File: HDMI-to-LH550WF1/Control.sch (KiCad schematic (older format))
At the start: 48 parts, among them P4 CONN_02X10, P5 CONN_01X03, U10 FXMA2104UMX, U11 STM32F103C8Tx, U9 FXMA2104UMX, Y1 8MHz

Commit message: C46 should be 0603
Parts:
- C46: footprint Capacitors_SMD:C_0402 -> Capacitors_SMD:C_0603
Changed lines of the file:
@@
 F 0 "C46" H 5710 1270 50  0000 L CNN
 F 1 "4.7uF" H 5710 1120 50  0000 L CNN
-F 2 "Capacitors_SMD:C_0402" H 5700 1200 50  0001 C CNN
+F 2 "Capacitors_SMD:C_0603" H 5700 1200 50  0001 C CNN
 F 3 "" H 5700 1200 50  0000 C CNN
 	1    5700 1200

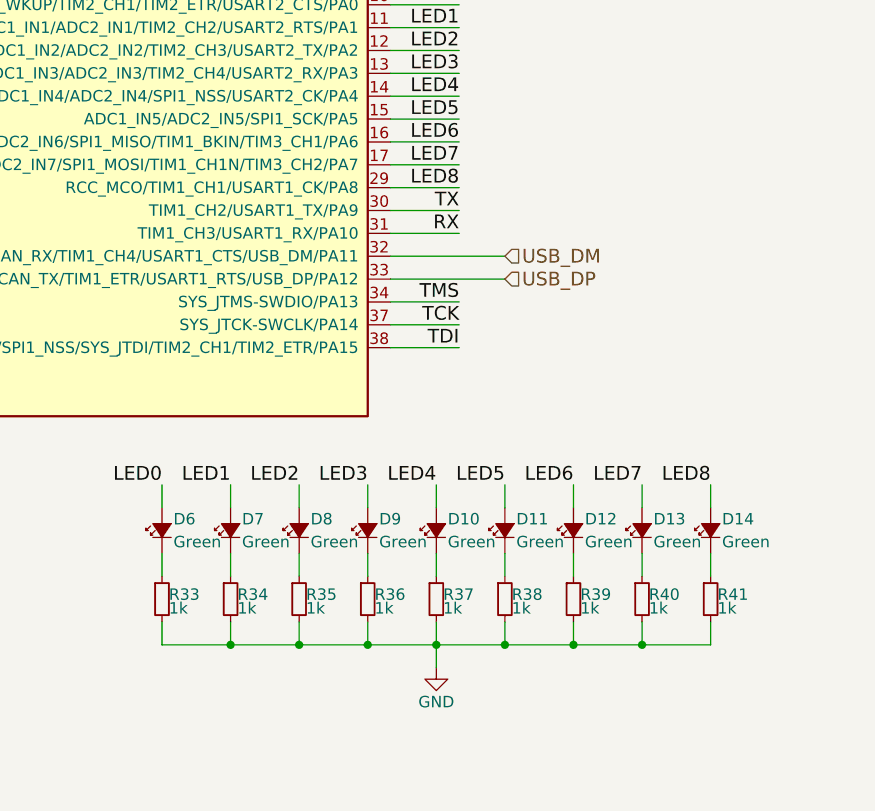
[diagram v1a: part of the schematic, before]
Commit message: Removed LED8
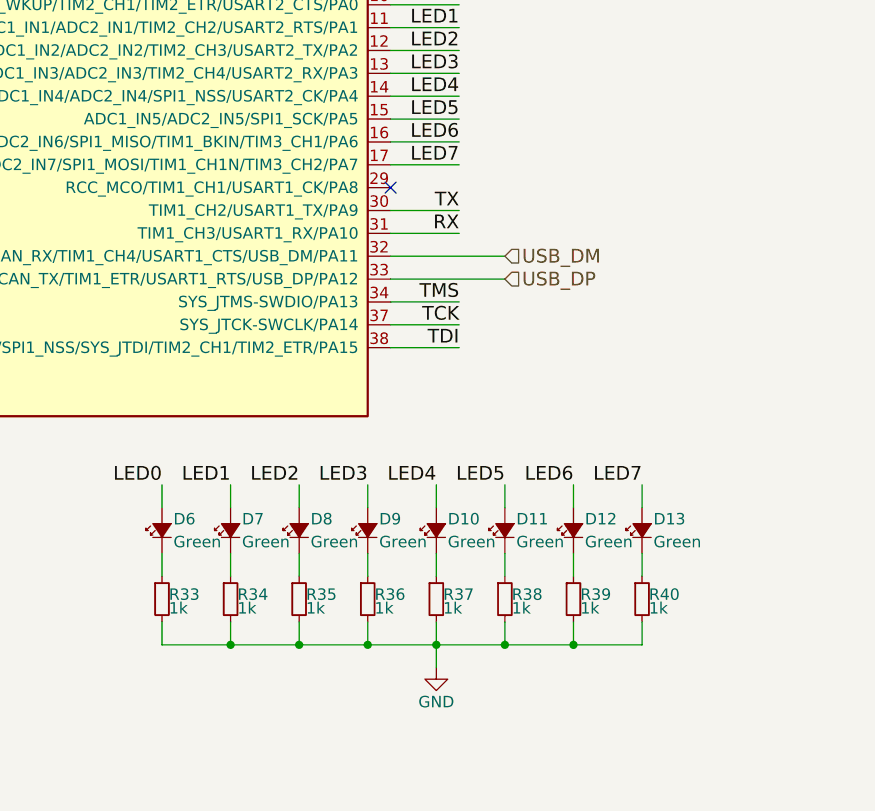
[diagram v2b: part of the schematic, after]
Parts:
- removed D14: Green, LEDs:LED_0603, symbol Led_Small
- removed R41: 1k, Resistors_SMD:R_0402, symbol R_Small
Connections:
- net labels removed: LED8
- wire segments 154 -> 150
- no-connect marks 23 -> 24
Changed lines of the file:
@@
-$EndComp
-$Comp
-L Led_Small D14
-U 1 1 58421F30
-P 10400 5700
-F 0 "D14" V 10450 5650 50  0000 R CNN
-F 1 "Green" V 10350 5650 50  0000 R CNN
-F 2 "LEDs:LED_0603" V 10400 5700 50  0001 C CNN
-F 3 "" V 10400 5700 50  0000 C CNN
-	1    10400 5700
-	0    -1   -1   0
-$EndComp
-$Comp
-L R_Small R41
-U 1 1 58422149
-P 10400 6000
-F 0 "R41" H 10430 6020 50  0000 L CNN
-F 1 "1k" H 10430 5960 50  0000 L CNN
-F 2 "Resistors_SMD:R_0402" H 10400 6000 50  0001 C CNN
-F 3 "" H 10400 6000 50  0000 C CNN
-	1    10400 6000
-	1    0    0    -1
 $EndComp
 $Comp
@@
 	8000 6100 8000 6200
 Wire Wire Line
-	8000 6200 10400 6200
-Wire Wire Line
-	10400 6200 10400 6100
-Wire Wire Line
-	10100 6100 10100 6200
-Connection ~ 10100 6200
-Wire Wire Line
-	9800 6100 9800 6200
+	10100 6200 10100 6100
+Wire Wire Line
+	9800 6200 9800 6100
 Connection ~ 9800 6200
 Wire Wire Line
-	9500 6100 9500 6200
+	9500 6200 9500 6100
 Connection ~ 9500 6200
 Wire Wire Line
@@
 Connection ~ 9200 6200
 Wire Wire Line
-	8900 6100 8900 6200
+	8900 6200 8900 6100
 Connection ~ 8900 6200
 Wire Wire Line
-	8600 6100 8600 6200
+	8600 6200 8600 6100
 Connection ~ 8600 6200
 Wire Wire Line
@@
 Wire Wire Line
 	10100 5800 10100 5900
-Wire Wire Line
-	10400 5800 10400 5900
 $Comp
 L GND #PWR0108
@@
 Text Label 10100 5500 2    60   ~ 0
 LED7
-Text Label 10400 5500 2    60   ~ 0
-LED8
-Wire Wire Line
-	10400 5500 10400 5600
 Wire Wire Line
 	10100 5500 10100 5600
@@
 Text Label 9300 4100 2    60   ~ 0
 LED7
-Text Label 9300 4200 2    60   ~ 0
-LED8
-Wire Wire Line
-	9300 4200 9000 4200
 Wire Wire Line
 	9000 4100 9300 4100
@@
 NoConn ~ 3200 4900
 NoConn ~ 3200 2500
+NoConn ~ 9000 4200
+Wire Wire Line
+	8000 6200 10100 6200
 $EndSCHEMATC
